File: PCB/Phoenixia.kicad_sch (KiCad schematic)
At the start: 218 parts, among them J2 Button, J5 Conn_01x03_Male, K0 Blank, K1 Blank, K10 Blank, K11 Blank, K12 Blank, K13 Blank, K14 Blank, K15 Blank, K16 Blank, K17 Blank, K18 Blank, K19 Blank, K2 Blank, K20 Blank, K21 Blank, K22 Blank, K23 Blank, K24 Blank, K25 Blank, K26 Blank, K27 Blank, K28 Blank, K29 Blank, K3 Blank, K30 Blank, K31 Blank, K32 Blank, K33 Blank, K34 Blank, K35 Blank, K36 Blank, K37 Blank, K38 Blank, K39 Blank, K4 Blank, K40 Blank, K41 Blank, K42 Blank, K43 Blank, K44 Blank, K45 Blank, K46 Blank, K47 Blank, K48 Blank, K49 Blank, K5 Blank, K50 Blank, K51 Blank, K52 Blank, K53 Blank, K54 Blank, K55 Blank, K56 Blank, K57 Blank, K58 Blank, K59 Blank, K6 Blank, K60 Blank, K61 Blank, K62 Blank, K63 Blank, K64 Blank, K65 Blank, K66 Blank, K67 Blank, K68 Blank, K69 Blank, K7 Blank, K70 Blank, K71 Blank, K72 Blank, K73 Blank, K74 Blank, K75 Blank, K76 Blank, K8 Blank, K9 Blank, U1 SOT-23-5 5.5V 3.3V 500mA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

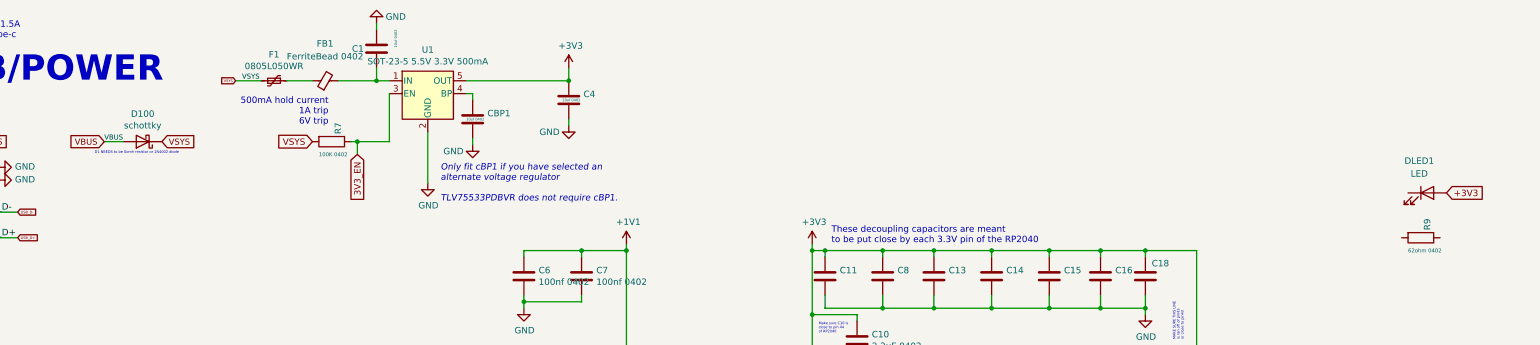
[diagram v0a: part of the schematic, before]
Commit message: Trace changes and teardrops
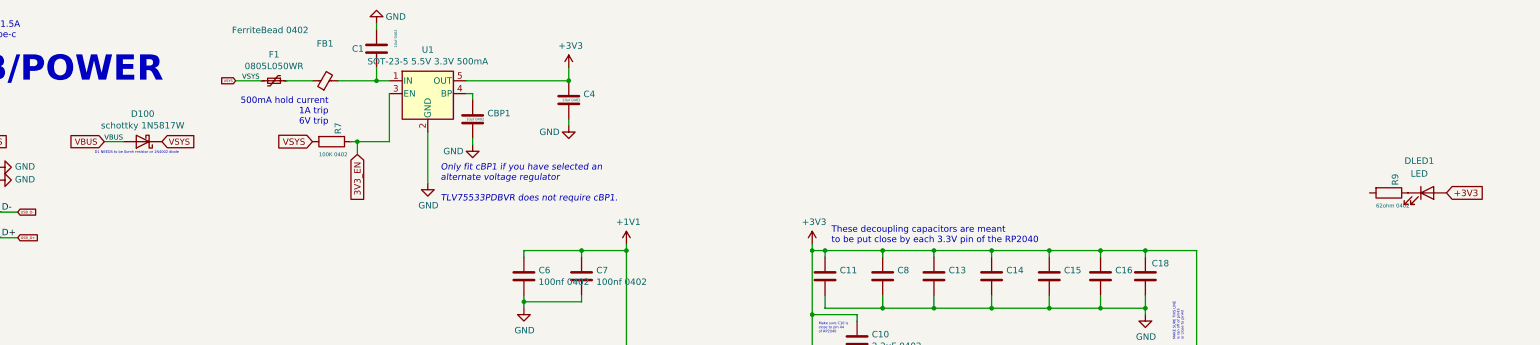
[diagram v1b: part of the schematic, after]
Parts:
- D100: value schottky -> schottky 1N5817W
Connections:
- net at DLED1.1 (K): now also R9.1
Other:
- moved on the sheet: R9
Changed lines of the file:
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@@
 			)
 		)
-		(property "Value" "schottky"
+		(property "Value" "schottky 1N5817W"
 			(at 81.915 36.1696 0)
 			(effects
@@
 	(symbol
 		(lib_id "Device:R")
-		(at 335.28 58.42 270)
+		(at 328.93 49.53 270)
 		(unit 1)
 		(exclude_from_sim no)
@@
 		(dnp no)
 		(property "Reference" "R9"
-			(at 336.55 54.61 0)
+			(at 330.2 45.72 0)
 			(effects
 				(font
@@
 		)
 		(property "Value" "62ohm 0402"
-			(at 332.74 60.96 90)
+			(at 326.39 52.07 90)
 			(effects
 				(font
@@
 		)
 		(property "Footprint" "Resistor_SMD:R_0402_1005Metric"
-			(at 335.28 56.642 90)
+			(at 328.93 47.752 90)
 			(effects
 				(font
@@
 		)
 		(property "Datasheet" ""
-			(at 335.28 58.42 0)
+			(at 328.93 49.53 0)
 			(effects
 				(font
@@
 		)
 		(property "Description" ""
-			(at 335.28 58.42 0)
+			(at 328.93 49.53 0)
 			(effects
 				(font
@@
 		)
 		(property "LCSC" " "
-			(at 335.28 58.42 0)
+			(at 328.93 49.53 0)
 			(effects
 				(font
@@
 		(on_board yes)
 		(dnp no)
-		(fields_autoplaced yes)
 		(property "Reference" "FB1"
 			(at 118.0592 19.939 90)
@@
 		)
 		(property "Value" "FerriteBead 0402"
-			(at 118.0592 22.479 90)
+			(at 107.188 17.272 90)
 			(effects
 				(font
